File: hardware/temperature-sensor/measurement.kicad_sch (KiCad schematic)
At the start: 1 part, among them IC1 SHT40-CD1B-R3

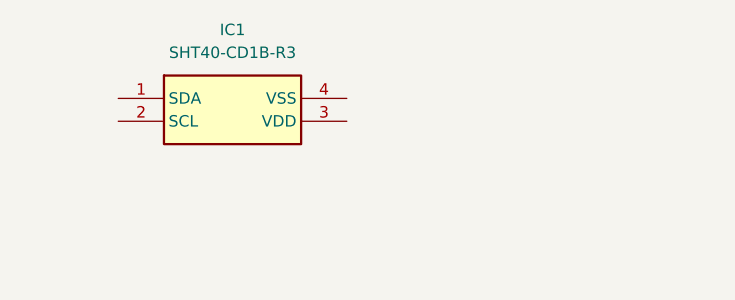
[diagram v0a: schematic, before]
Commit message: work on temperature sensor
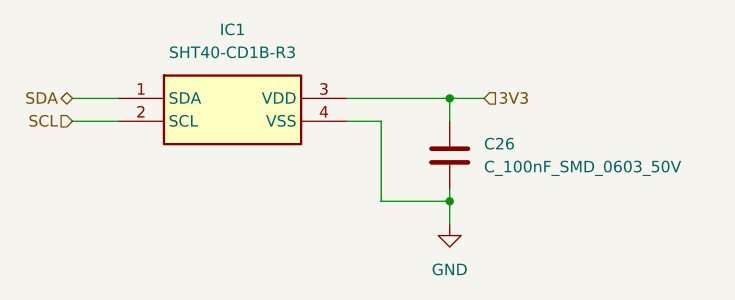
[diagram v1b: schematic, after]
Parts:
- added C26: C_100nF_SMD_0603_50V, benediktibk:C_0603_1608Metric_Pad1.08x0.95mm_HandSolder, symbol benediktibk:C_100nF_SMD_0603_50V
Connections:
- net SDA: now reaches IC1.1 (SDA)
- net SCL: now reaches IC1.2 (SCL)
- net 3V3: now reaches IC1.3 (VDD)
- net 3V3: now also C26.1
- net GND: now reaches IC1.4 (VSS)
- net GND: now also C26.2
